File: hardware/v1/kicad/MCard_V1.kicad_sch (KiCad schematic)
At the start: 0 parts

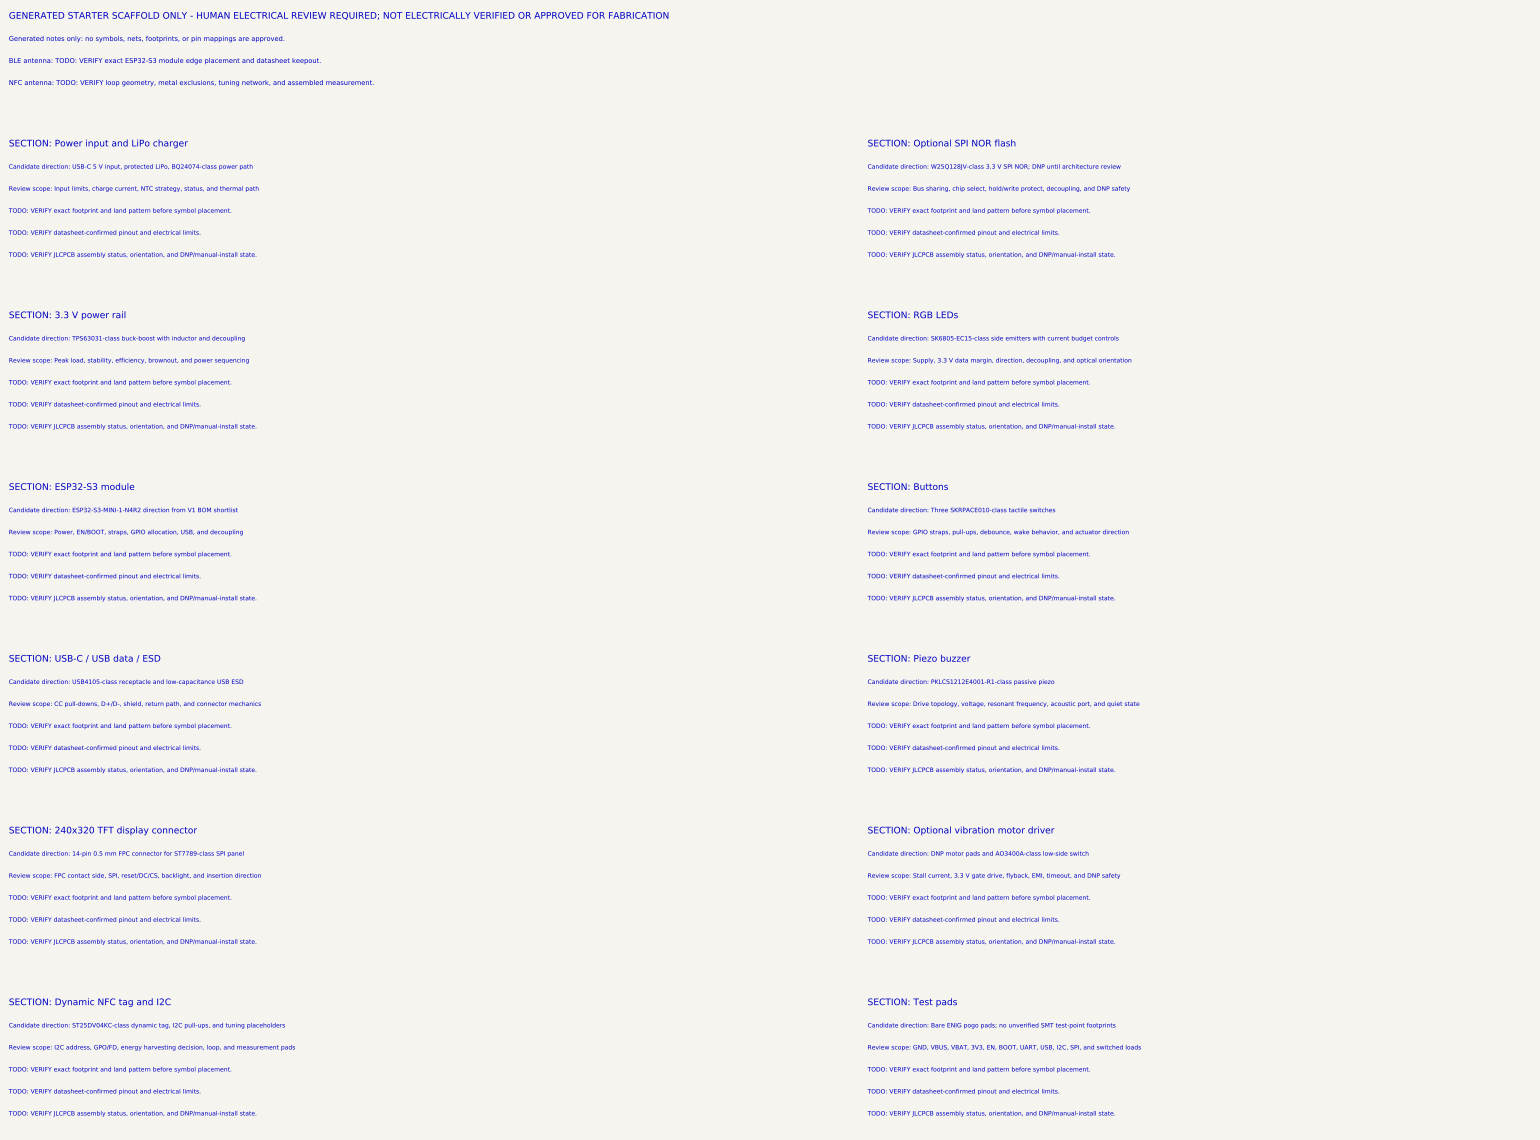
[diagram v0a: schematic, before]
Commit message: Patch V1 KiCad scaffold with placement constraints
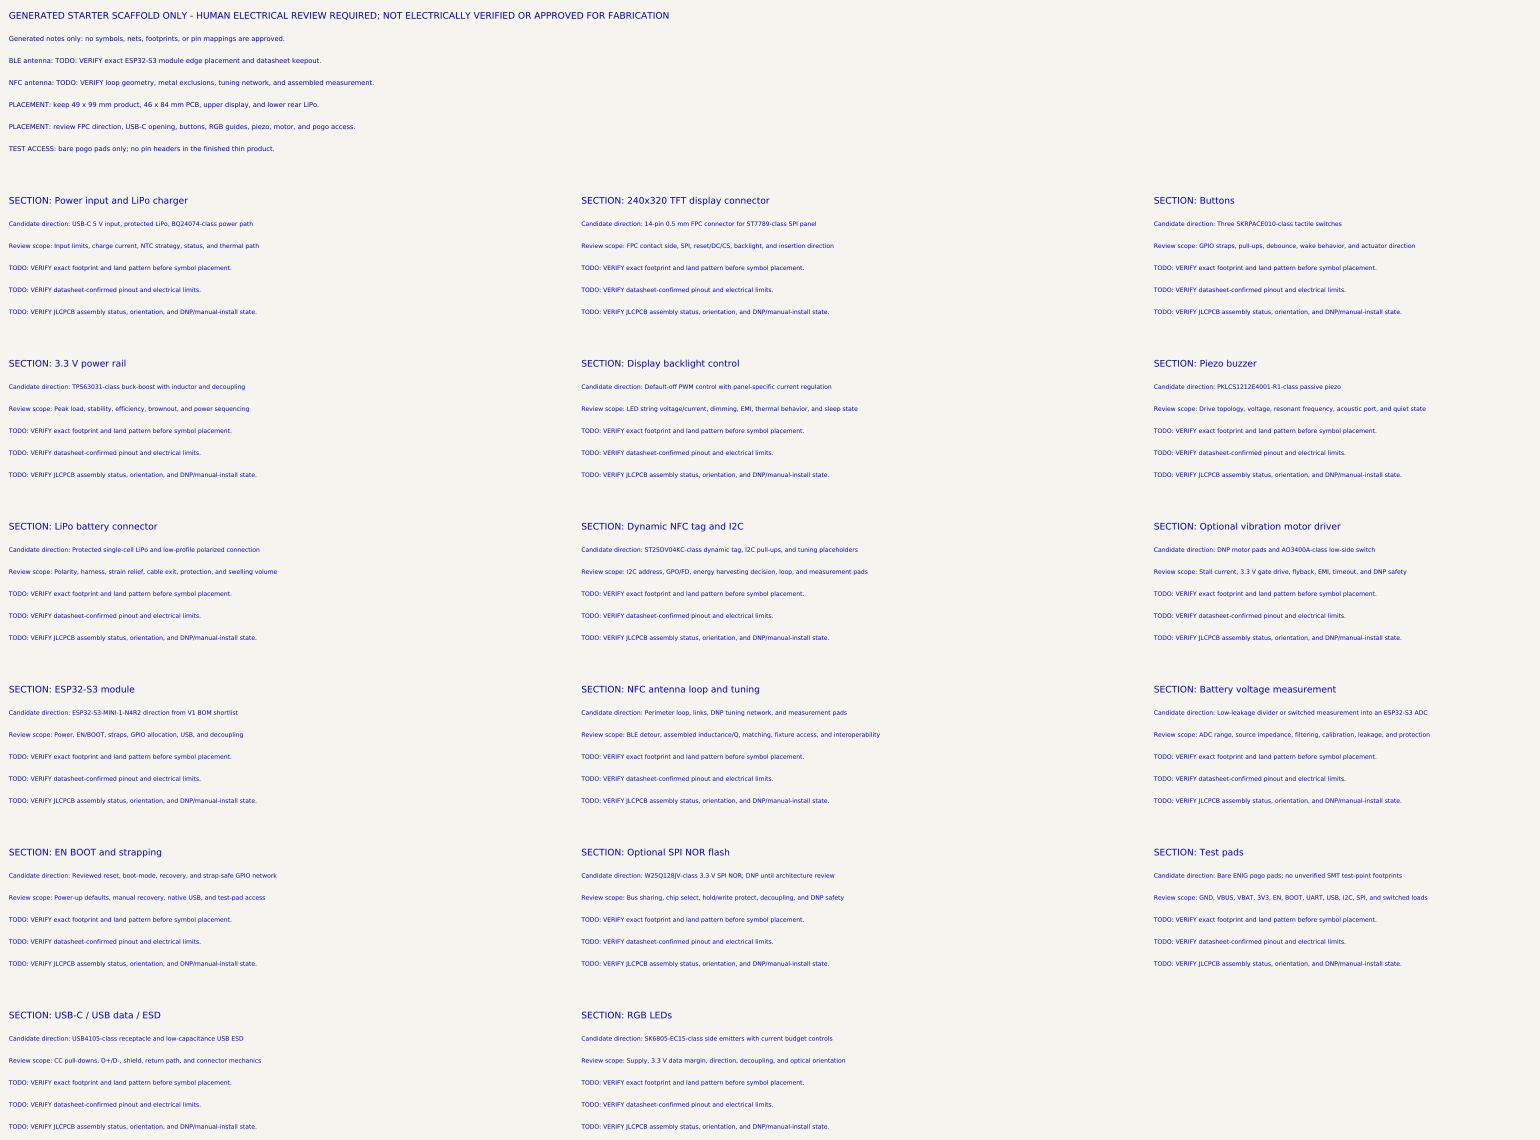
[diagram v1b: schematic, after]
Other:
- note added: "Candidate direction: Default-off PWM control with panel-specific current regulation"
- note added: "Candidate direction: Low-leakage divider or switched measurement into an ESP32-S3 ADC"
- note added: "Candidate direction: Perimeter loop, links, DNP tuning network, and measurement pads"
- note added: "Candidate direction: Protected single-cell LiPo and low-profile polarized connection"
- note added: "Candidate direction: Reviewed reset, boot-mode, recovery, and strap-safe GPIO network"
- note added: "PLACEMENT: keep 49 x 99 mm product, 46 x 84 mm PCB, upper display, and lower rear LiPo."
- note added: "PLACEMENT: review FPC direction, USB-C opening, buttons, RGB guides, piezo, motor, and pogo access."
- note added: "Review scope: ADC range, source impedance, filtering, calibration, leakage, and protection"
- note added: "Review scope: BLE detour, assembled inductance/Q, matching, fixture access, and interoperability"
- note added: "Review scope: LED string voltage/current, dimming, EMI, thermal behavior, and sleep state"
- note added: "Review scope: Polarity, harness, strain relief, cable exit, protection, and swelling volume"
- note added: "Review scope: Power-up defaults, manual recovery, native USB, and test-pad access"
- note added: "SECTION: Battery voltage measurement"
- note added: "SECTION: Display backlight control"
- note added: "SECTION: EN BOOT and strapping"
- note added: "SECTION: LiPo battery connector"
- note added: "SECTION: NFC antenna loop and tuning"
- note added: "TEST ACCESS: bare pogo pads only; no pin headers in the finished thin product."
